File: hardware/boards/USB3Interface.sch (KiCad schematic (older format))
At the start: 6 parts, among them J2 USB3_Micro_B_Amphenol, U1 ECP5UM5G-381caBGA, U3 CYUSB3014, U6 128MiB

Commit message: Added a bunch of stuff having to do with JTAG and the FPGA flash / bring up
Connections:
- net at U3.C1 (GPIO[54]): now also U6.1 (~CS)
- net at U3.C2 (GPIO[55]): now also U6.2 (DO/IO1)
- net at U3.D4 (GPIO[53]): now also U6.6 (CLK)
- net at U3.D5 (GPIO[56]): now also U6.5 (DI/IO0)
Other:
- moved on the sheet: U6B
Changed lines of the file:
@@
 L lethalbit-memory:W25N01GVZEIG U?
 U 2 1 5FF1D42C
-P 4350 6800
+P 6400 5900
 AR Path="/5EF66251/5FF1D42C" Ref="U?"  Part="2"
 AR Path="/5F2CAFD2/5FF1D42C" Ref="U6"  Part="2"
-F 0 "U6" H 4375 7024 39  0000 C CNN
-F 1 "128MiB" H 4375 6949 39  0000 C CNN
-F 2 "lethalbit-memory:WSON-8-1EP-6.0x8.0mm" H 4350 6950 39  0001 C CNN
-F 3 "https://www.winbond.com/resource-files/w25n01gv%20revl%20050918%20unsecured.pdf" H 4350 6950 39  0001 C CNN
-F 4 "Winbond" H 4350 6800 50  0001 C CNN "MFR"
-F 5 "W25N01GVZEIG" H 4350 6800 50  0001 C CNN "MPN"
-	2    4350 6800
+F 0 "U6" H 6425 6124 39  0000 C CNN
+F 1 "128MiB" H 6425 6049 39  0000 C CNN
+F 2 "lethalbit-memory:WSON-8-1EP-6.0x8.0mm" H 6400 6050 39  0001 C CNN
+F 3 "https://www.winbond.com/resource-files/w25n01gv%20revl%20050918%20unsecured.pdf" H 6400 6050 39  0001 C CNN
+F 4 "Winbond" H 6400 5900 50  0001 C CNN "MFR"
+F 5 "W25N01GVZEIG" H 6400 5900 50  0001 C CNN "MPN"
+	2    6400 5900
 	1    0    0    -1
 $EndComp
@@
 	1    0    0    -1
 $EndComp
+Wire Wire Line
+	6950 6050 7150 6050
+Wire Wire Line
+	7150 6050 7150 5800
+Wire Wire Line
+	7150 5800 5500 5800
+Wire Wire Line
+	5500 5800 5500 5850
+Wire Wire Line
+	5500 5850 5050 5850
+Wire Wire Line
+	5900 5950 5050 5950
+Wire Wire Line
+	5900 6050 5050 6050
+Wire Wire Line
+	6950 6150 7100 6150
+Wire Wire Line
+	7100 6150 7100 6250
+Wire Wire Line
+	7100 6250 5800 6250
+Wire Wire Line
+	5800 6250 5800 6150
+Wire Wire Line
+	5800 6150 5050 6150
 $EndSCHEMATC

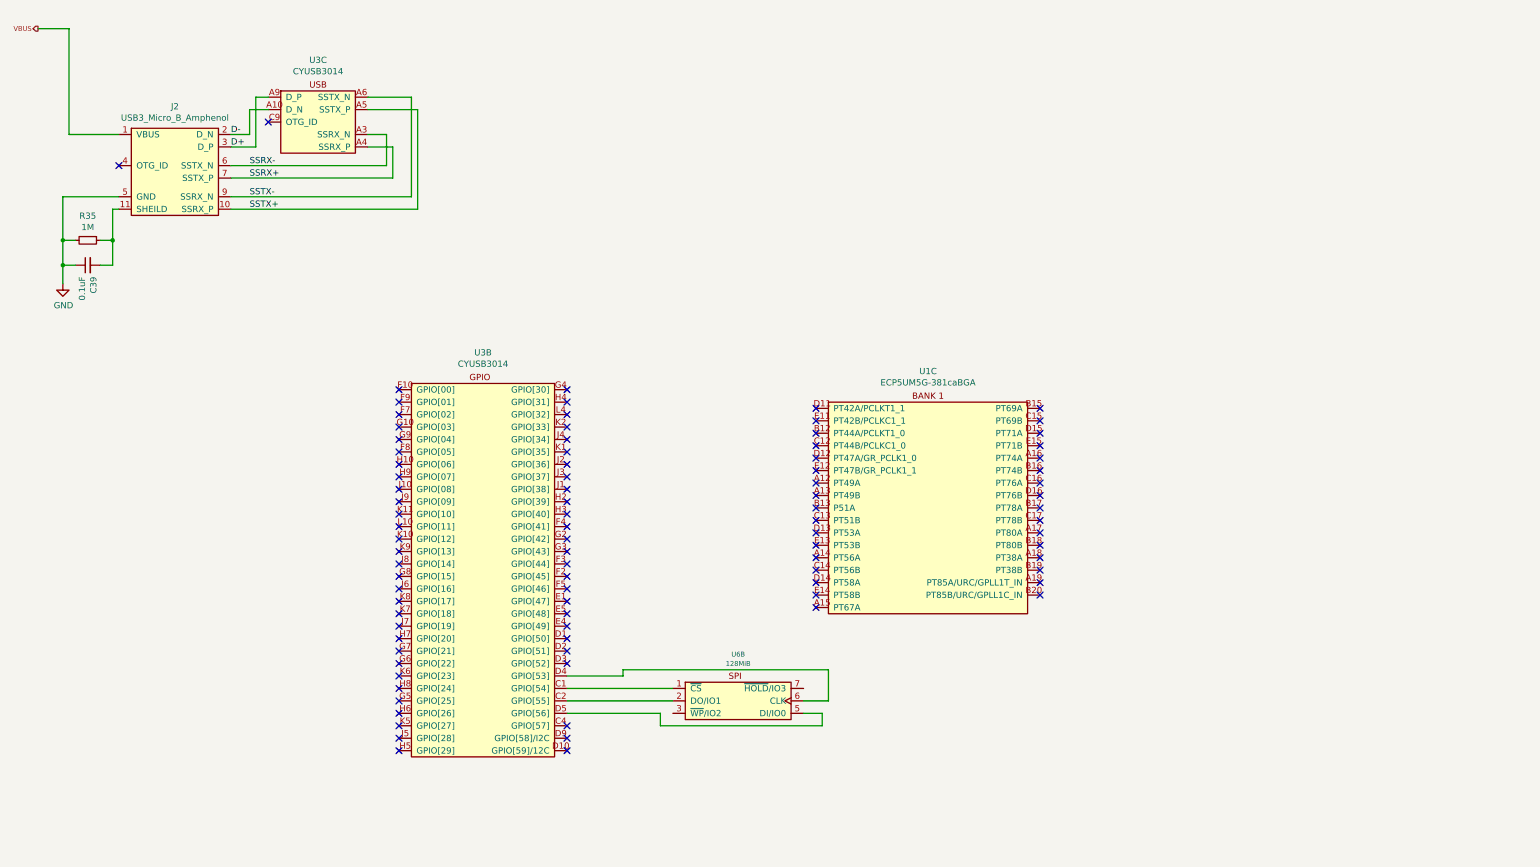
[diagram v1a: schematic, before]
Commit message: Some ERC cleanup
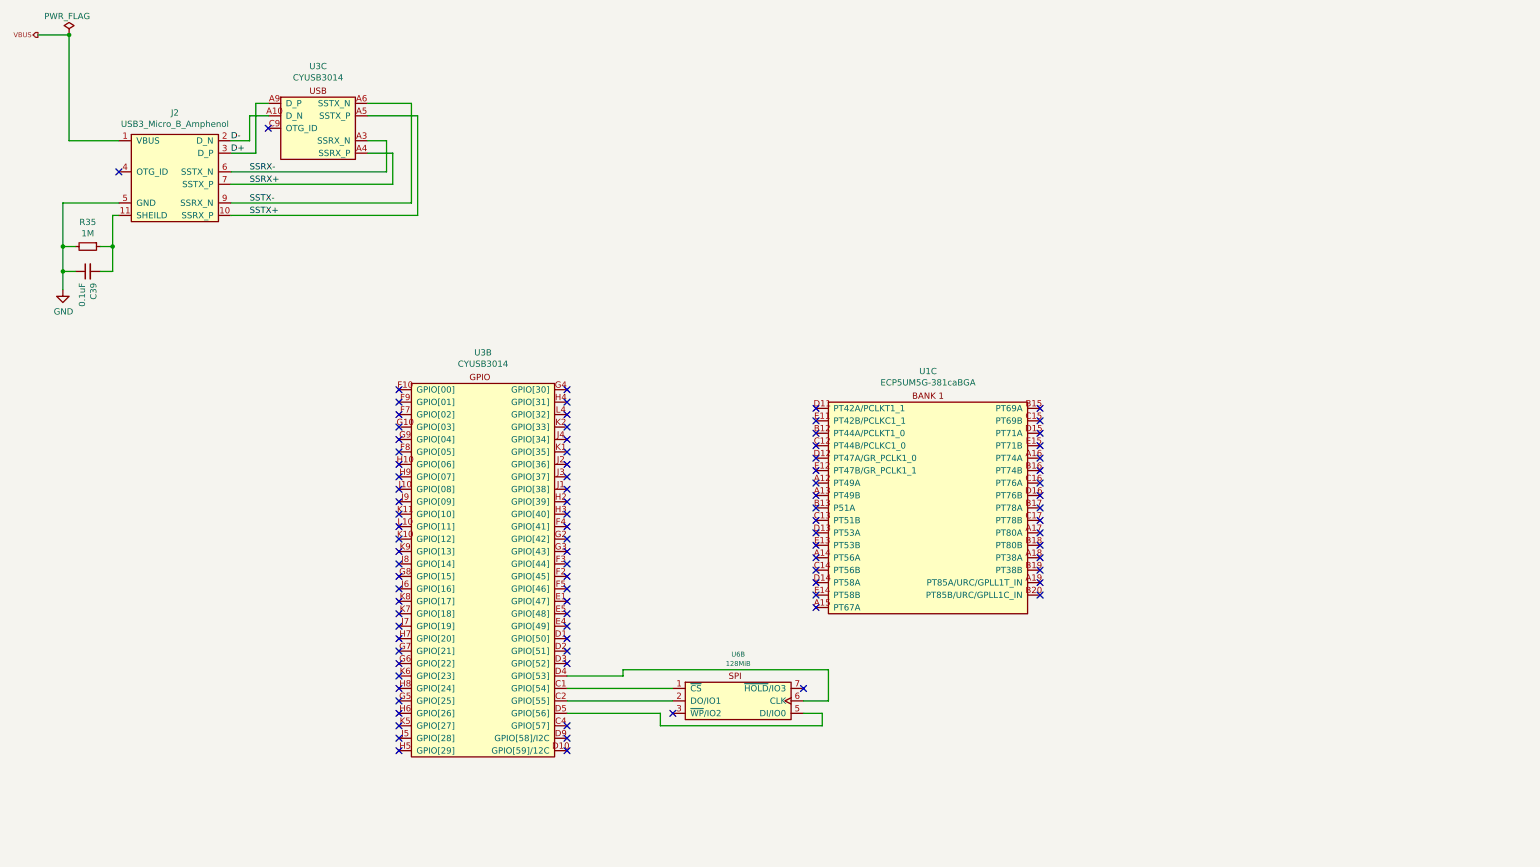
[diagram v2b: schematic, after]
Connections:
- no-connect marks 91 -> 93
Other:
- moved on the sheet: C39, J2, R35, U3C
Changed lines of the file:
@@
 L lethalbit:CYUSB3014 U3
 U 3 1 5F3336EC
-P 3050 1700
-F 0 "U3" H 3050 2498 50  0000 C CNN
-F 1 "CYUSB3014" H 3050 2407 50  0000 C CNN
-F 2 "lethalbit:BGA-121_11x11_10.0x10.0mm" H 3050 2400 50  0001 C CNN
-F 3 "https://www.cypress.com/file/140296/download" H 3050 2400 50  0001 C CNN
-F 4 "Cypress" H 3050 1700 50  0001 C CNN "MFR"
-F 5 " CYUSB3014-BZXI" H 3050 1700 50  0001 C CNN "MPN"
-F 6 "428-3130-ND" H 3050 1700 50  0001 C CNN "DIGIKEY_PN"
-	3    3050 1700
+P 3050 1750
+F 0 "U3" H 3050 2548 50  0000 C CNN
+F 1 "CYUSB3014" H 3050 2457 50  0000 C CNN
+F 2 "lethalbit:BGA-121_11x11_10.0x10.0mm" H 3050 2450 50  0001 C CNN
+F 3 "https://www.cypress.com/file/140296/download" H 3050 2450 50  0001 C CNN
+F 4 "Cypress" H 3050 1750 50  0001 C CNN "MFR"
+F 5 " CYUSB3014-BZXI" H 3050 1750 50  0001 C CNN "MPN"
+F 6 "428-3130-ND" H 3050 1750 50  0001 C CNN "DIGIKEY_PN"
+	3    3050 1750
 	1    0    0    -1
 $EndComp
@@
 L lethalbit:USB3_Micro_B_Amphenol J2
 U 1 1 5F8A43B9
-P 1900 1800
-F 0 "J2" H 1900 2325 50  0000 C CNN
-F 1 "USB3_Micro_B_Amphenol" H 1900 2234 50  0000 C CNN
-F 2 "lethalbit:USB3_Micro_B_Amphenol" H 1900 2250 50  0001 C CNN
-F 3 "https://www.amphenol-icc.com/media/wysiwyg/files/drawing/gsb343k33hr.pdf" H 1900 2250 50  0001 C CNN
-F 4 "Amphenol" H 1900 2250 50  0001 C CNN "MFR"
-F 5 "GSB343K33HR" H 1900 2250 50  0001 C CNN "MPN"
-F 6 "GSB343K33HRCT-ND" H 1900 1800 50  0001 C CNN "DIGIKEY_PN"
-	1    1900 1800
-	1    0    0    -1
-$EndComp
-Wire Wire Line
-	2350 1500 2500 1500
-Wire Wire Line
-	2500 1500 2500 1300
-Wire Wire Line
-	2500 1300 2650 1300
-Wire Wire Line
-	2350 1600 2550 1600
-Wire Wire Line
-	2550 1600 2550 1200
-Wire Wire Line
-	2550 1200 2650 1200
+P 1900 1850
+F 0 "J2" H 1900 2375 50  0000 C CNN
+F 1 "USB3_Micro_B_Amphenol" H 1900 2284 50  0000 C CNN
+F 2 "lethalbit:USB3_Micro_B_Amphenol" H 1900 2300 50  0001 C CNN
+F 3 "https://www.amphenol-icc.com/media/wysiwyg/files/drawing/gsb343k33hr.pdf" H 1900 2300 50  0001 C CNN
+F 4 "Amphenol" H 1900 2300 50  0001 C CNN "MFR"
+F 5 "GSB343K33HR" H 1900 2300 50  0001 C CNN "MPN"
+F 6 "GSB343K33HRCT-ND" H 1900 1850 50  0001 C CNN "DIGIKEY_PN"
+	1    1900 1850
+	1    0    0    -1
+$EndComp
+Wire Wire Line
+	2350 1550 2500 1550
+Wire Wire Line
+	2500 1550 2500 1350
+Wire Wire Line
+	2500 1350 2650 1350
+Wire Wire Line
+	2350 1650 2550 1650
+Wire Wire Line
+	2550 1650 2550 1250
+Wire Wire Line
+	2550 1250 2650 1250
 $Comp
 L power:GND #PWR0118
 U 1 1 5EDDAAAC
-P 1000 2700
-F 0 "#PWR0118" H 1000 2450 50  0001 C CNN
-F 1 "GND" H 1005 2527 50  0000 C CNN
-F 2 "" H 1000 2700 50  0001 C CNN
-F 3 "" H 1000 2700 50  0001 C CNN
-	1    1000 2700
-	1    0    0    -1
-$EndComp
-Wire Wire Line
-	1450 2000 1000 2000
-Wire Wire Line
-	1000 2000 1000 2350
+P 1000 2750
+F 0 "#PWR0118" H 1000 2500 50  0001 C CNN
+F 1 "GND" H 1005 2577 50  0000 C CNN
+F 2 "" H 1000 2750 50  0001 C CNN
+F 3 "" H 1000 2750 50  0001 C CNN
+	1    1000 2750
+	1    0    0    -1
+$EndComp
+Wire Wire Line
+	1450 2050 1000 2050
+Wire Wire Line
+	1000 2050 1000 2400
 $Comp
 L Device:R_Small R?
 U 1 1 5EDFF9C0
-P 1200 2350
+P 1200 2400
 AR Path="/5EDF9F51/5EDFF9C0" Ref="R?"  Part="1"
 AR Path="/5F2CAFD2/5EDFF9C0" Ref="R35"  Part="1"
-F 0 "R35" V 1004 2350 50  0000 C CNN
-F 1 "1M" V 1095 2350 50  0000 C CNN
-F 2 "Resistor_SMD:R_0603_1608Metric" H 1200 2350 50  0001 C CNN
-F 3 "~" H 1200 2350 50  0001 C CNN
-F 4 "Vishay Dale" V 1200 2350 50  0001 C CNN "MFR"
-F 5 "CRCW06031M00FKEA" V 1200 2350 50  0001 C CNN "MPN"
-	1    1200 2350
+F 0 "R35" V 1004 2400 50  0000 C CNN
+F 1 "1M" V 1095 2400 50  0000 C CNN
+F 2 "Resistor_SMD:R_0603_1608Metric" H 1200 2400 50  0001 C CNN
+F 3 "~" H 1200 2400 50  0001 C CNN
+F 4 "Vishay Dale" V 1200 2400 50  0001 C CNN "MFR"
+F 5 "CRCW06031M00FKEA" V 1200 2400 50  0001 C CNN "MPN"
+	1    1200 2400
 	0    1    1    0
 $EndComp
@@
 L Device:C_Small C?
 U 1 1 5EDFF9C8
-P 1200 2550
+P 1200 2600
 AR Path="/5EDF9F51/5EDFF9C8" Ref="C?"  Part="1"
 AR Path="/5F2CAFD2/5EDFF9C8" Ref="C39"  Part="1"
-F 0 "C39" H 1108 2504 50  0000 R CNN
-F 1 "0.1uF" H 1108 2595 50  0000 R CNN
-F 2 "Capacitor_SMD:C_0603_1608Metric" H 1200 2550 50  0001 C CNN
-F 3 "~" H 1200 2550 50  0001 C CNN
-F 4 "KEMET" V 1200 2550 50  0001 C CNN "MFR"
-F 5 "C0603C104M5RACTU" V 1200 2550 50  0001 C CNN "MPN"
-	1    1200 2550
+F 0 "C39" H 1108 2554 50  0000 R CNN
+F 1 "0.1uF" H 1108 2645 50  0000 R CNN
+F 2 "Capacitor_SMD:C_0603_1608Metric" H 1200 2600 50  0001 C CNN
+F 3 "~" H 1200 2600 50  0001 C CNN
+F 4 "KEMET" V 1200 2600 50  0001 C CNN "MFR"
+F 5 "C0603C104M5RACTU" V 1200 2600 50  0001 C CNN "MPN"
+	1    1200 2600
 	0    -1   -1   0
 $EndComp
 Wire Wire Line
-	1100 2550 1000 2550
-Connection ~ 1000 2550
-Wire Wire Line
-	1000 2550 1000 2700
-Wire Wire Line
-	1100 2350 1000 2350
-Connection ~ 1000 2350
-Wire Wire Line
-	1000 2350 1000 2550
-Wire Wire Line
-	1450 2100 1400 2100
-Wire Wire Line
-	1400 2100 1400 2350
-Wire Wire Line
-	1400 2550 1300 2550
-Wire Wire Line
-	1300 2350 1400 2350
-Connection ~ 1400 2350
-Wire Wire Line
-	1400 2350 1400 2550
-NoConn ~ 1450 1750
-NoConn ~ 2650 1400
+	1100 2600 1000 2600
+Connection ~ 1000 2600
+Wire Wire Line
+	1000 2600 1000 2750
+Wire Wire Line
+	1100 2400 1000 2400
+Connection ~ 1000 2400
+Wire Wire Line
+	1000 2400 1000 2600
+Wire Wire Line
+	1450 2150 1400 2150
+Wire Wire Line
+	1400 2150 1400 2400
+Wire Wire Line
+	1400 2600 1300 2600
+Wire Wire Line
+	1300 2400 1400 2400
+Connection ~ 1400 2400
+Wire Wire Line
+	1400 2400 1400 2600
+NoConn ~ 1450 1800
+NoConn ~ 2650 1450
 NoConn ~ 3700 3550
 NoConn ~ 3700 3650
@@
 NoConn ~ 8850 3800
 NoConn ~ 8850 3700
-Text HLabel 800  650  0    39   Output ~ 0
+Text HLabel 800  700  0    39   Output ~ 0
 VBUS
 Wire Wire Line
-	1050 650  1050 1500
-Wire Wire Line
-	1050 1500 1450 1500
-Wire Wire Line
-	800  650  1050 650
-Wire Wire Line
-	2350 1750 3600 1750
-Wire Wire Line
-	3600 1750 3600 1500
-Wire Wire Line
-	3600 1500 3450 1500
-Wire Wire Line
-	2350 1850 3650 1850
-Wire Wire Line
-	3650 1850 3650 1600
-Wire Wire Line
-	3650 1600 3450 1600
-Wire Wire Line
-	2350 2000 3800 2000
-Wire Wire Line
-	3800 2000 3800 1200
-Wire Wire Line
-	3800 1200 3450 1200
-Wire Wire Line
-	2350 2100 3850 2100
-Wire Wire Line
-	3850 2100 3850 1300
-Wire Wire Line
-	3850 1300 3450 1300
+	1050 700  1050 1550
+Wire Wire Line
+	1050 1550 1450 1550
+Wire Wire Line
+	800  700  1050 700
+Wire Wire Line
+	2350 1800 3600 1800
+Wire Wire Line
+	3600 1800 3600 1550
+Wire Wire Line
+	3600 1550 3450 1550
+Wire Wire Line
+	2350 1900 3650 1900
+Wire Wire Line
+	3650 1900 3650 1650
+Wire Wire Line
+	3650 1650 3450 1650
+Wire Wire Line
+	2350 2050 3800 2050
+Wire Wire Line
+	3800 2050 3800 1250
+Wire Wire Line
+	3800 1250 3450 1250
+Wire Wire Line
+	2350 2150 3850 2150
+Wire Wire Line
+	3850 2150 3850 1350
+Wire Wire Line
+	3850 1350 3450 1350
 NoConn ~ 7050 4700
-Text Label 2500 1750 0    50   ~ 0
+Text Label 2500 1800 0    50   ~ 0
 SSRX-
-Text Label 2500 1850 0    50   ~ 0
+Text Label 2500 1900 0    50   ~ 0
 SSRX+
-Text Label 2500 2000 0    50   ~ 0
+Text Label 2500 2050 0    50   ~ 0
 SSTX-
-Text Label 2500 2100 0    50   ~ 0
+Text Label 2500 2150 0    50   ~ 0
 SSTX+
-Text Label 2350 1600 0    50   ~ 0
+Text Label 2350 1650 0    50   ~ 0
 D+
-Text Label 2350 1500 0    50   ~ 0
+Text Label 2350 1550 0    50   ~ 0
 D-
 $Comp
@@
 Wire Wire Line
 	5800 6150 5050 6150
+$Comp
+L power:PWR_FLAG #FLG?
+U 1 1 605EDABA
+P 1050 700
+AR Path="/605EDABA" Ref="#FLG?"  Part="1"
+AR Path="/5F2CAFD2/605EDABA" Ref="#FLG0108"  Part="1"
+F 0 "#FLG0108" H 1050 775 50  0001 C CNN
+F 1 "PWR_FLAG" H 850 850 50  0000 L CNN
+F 2 "" H 1050 700 50  0001 C CNN
+F 3 "~" H 1050 700 50  0001 C CNN
+	1    1050 700
+	1    0    0    -1
+$EndComp
+Connection ~ 1050 700
+NoConn ~ 6950 5950
+NoConn ~ 5900 6150
 $EndSCHEMATC

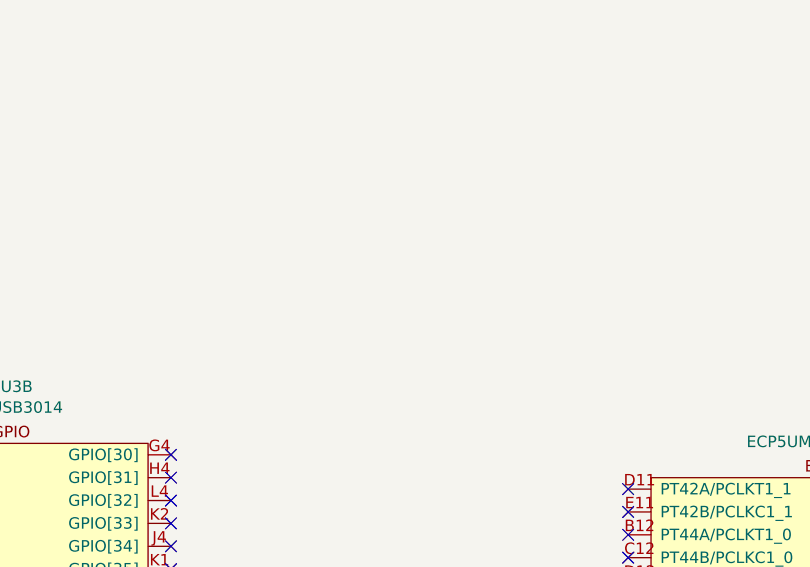
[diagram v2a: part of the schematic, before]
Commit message: Resized some nested schematics and pulled the GPIF II interrupt line out from the boot config block into the USB 3 interface
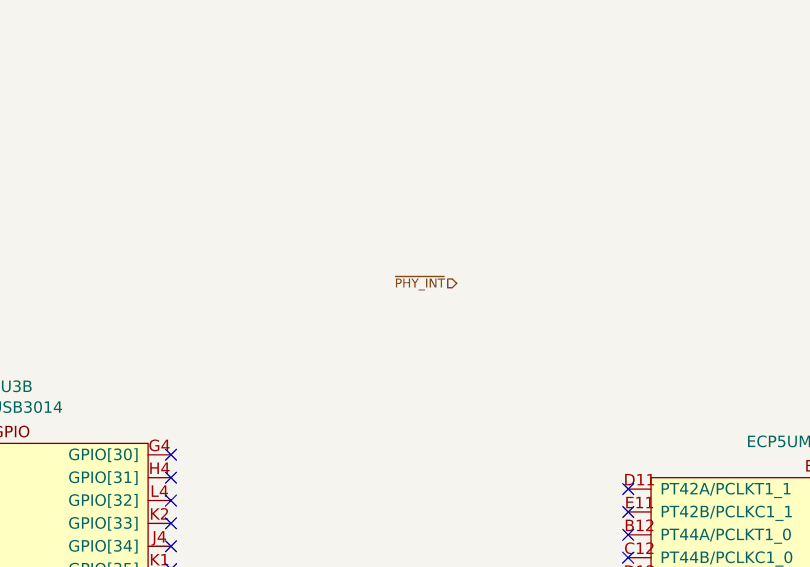
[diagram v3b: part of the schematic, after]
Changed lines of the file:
@@
 $Descr A3 16535 11693
 encoding utf-8
-Sheet 2 11
+Sheet 11 11
 Title "lethallink"
 Date "2020-06-13"
@@
 NoConn ~ 6950 5950
 NoConn ~ 5900 6150
+Text HLabel 6300 2800 0    39   Input ~ 0
+~PHY_INT
 $EndSCHEMATC
